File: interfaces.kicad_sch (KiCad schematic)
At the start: 20 parts

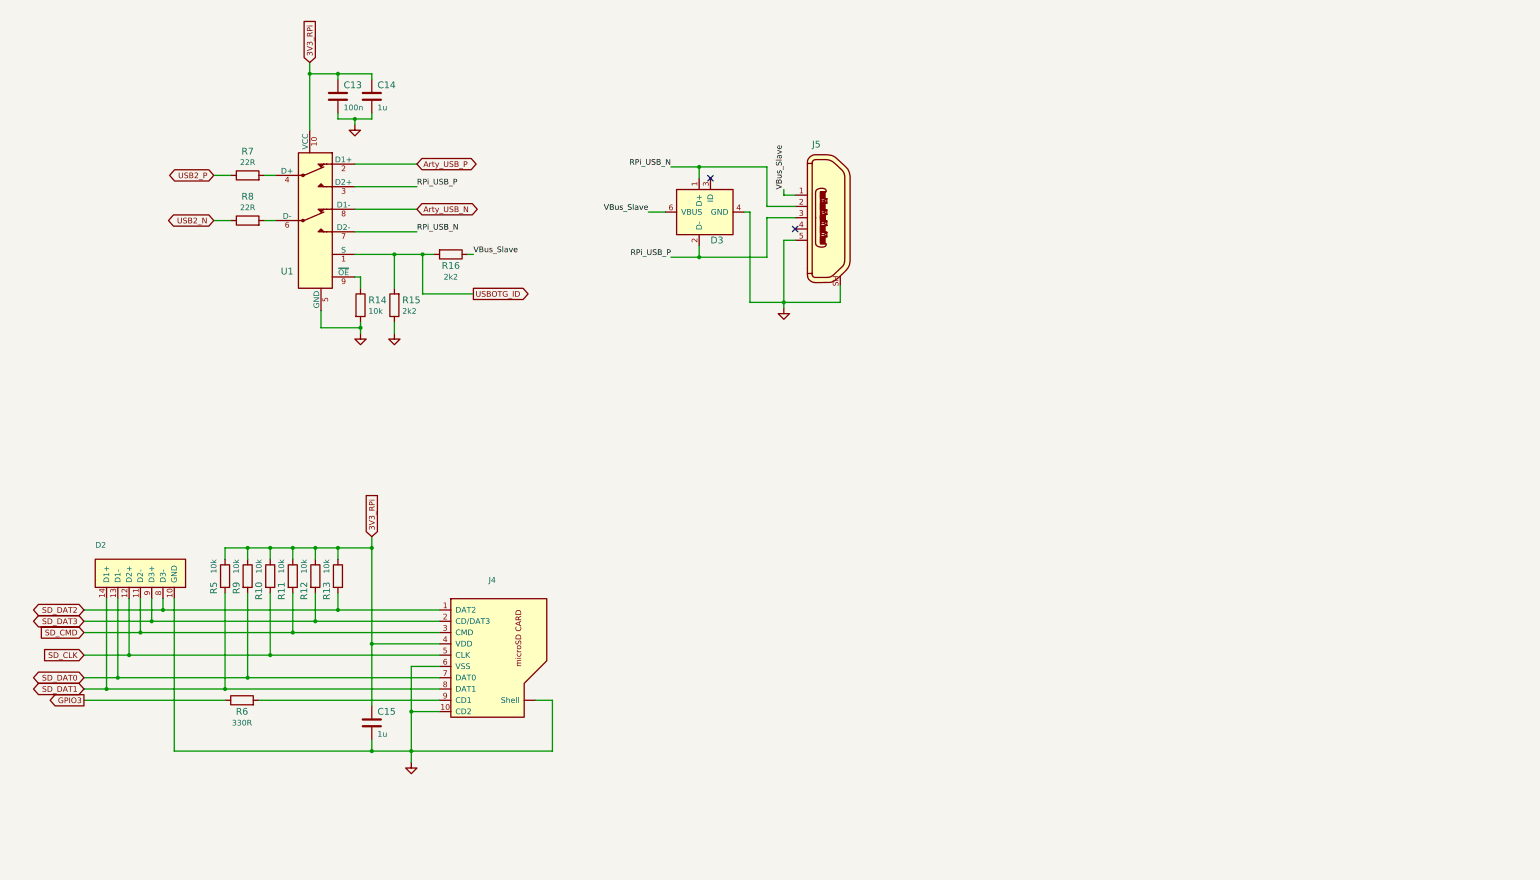
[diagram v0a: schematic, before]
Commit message: Exchanged flyback to CUI DCDC converter on schematics. Added logos.
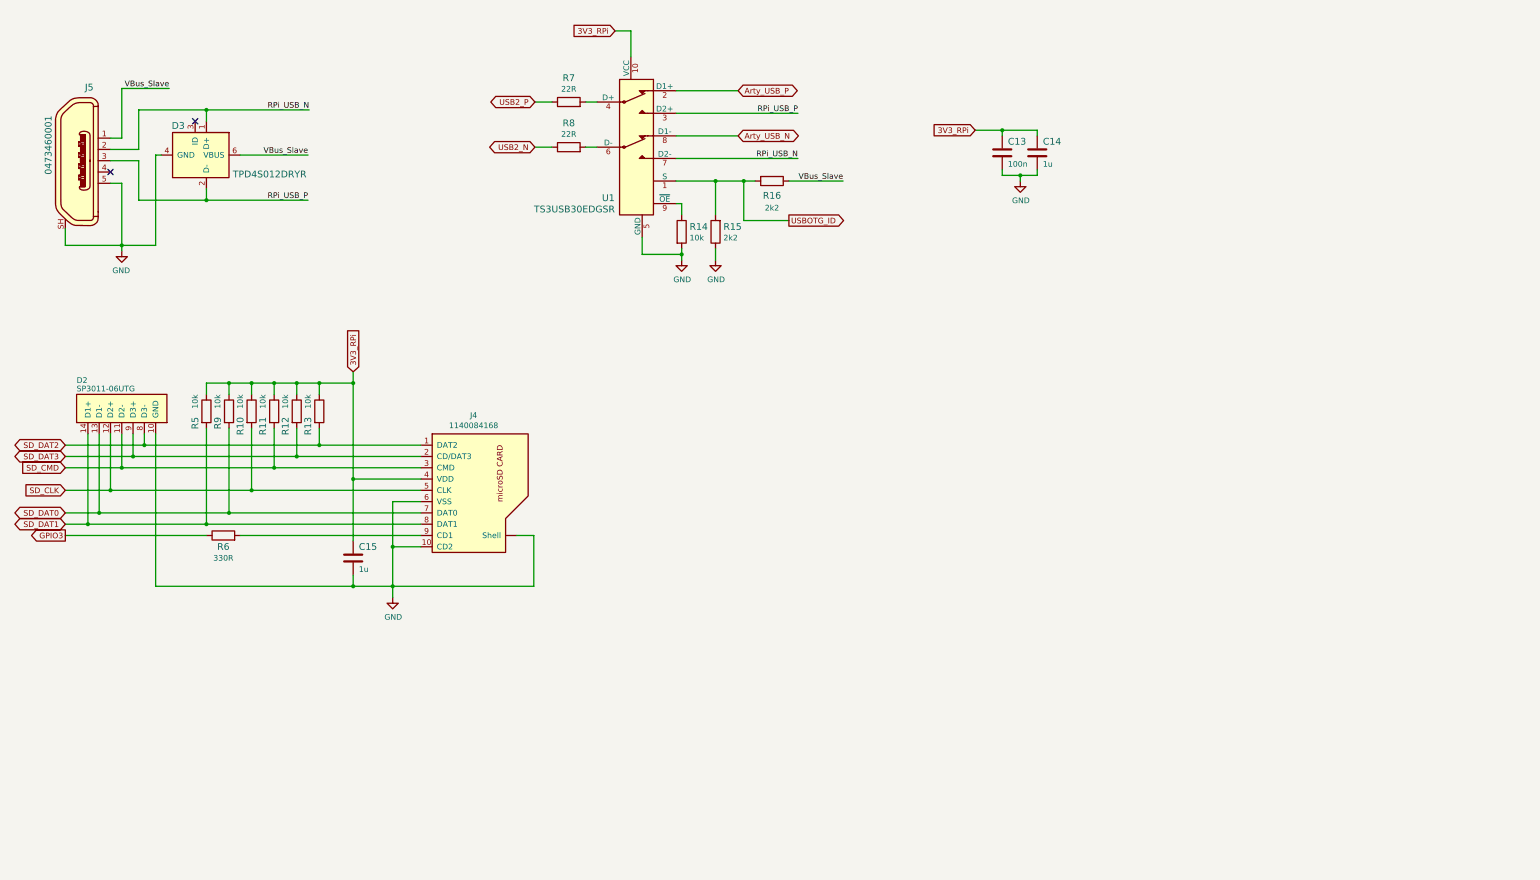
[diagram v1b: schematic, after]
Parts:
- C13: value (none) -> C_100n_0402; footprint scalenode-footprints: -> scalenode-footprints:0402-cap
- C14, C15: value (none) -> C_1u_0402; footprint scalenode-footprints: -> scalenode-footprints:0402-cap
- D2: value (none) -> SP3011-06UTG; footprint scalenode-footprints: -> scalenode-footprints:SON50P350X135X55-14N
- D3: value (none) -> TPD4S012DRYR; footprint scalenode-footprints: -> scalenode-footprints:UFDFN-6_1.45x1mm
- J4: value (none) -> 1140084168; footprint scalenode-footprints: -> scalenode-footprints:MicroSD_1140084168
- J5: value (none) -> 0473460001; footprint scalenode-footprints: -> scalenode-footprints:USB_Micro_B_Female_0473460001
- R10, R11, R12, R13, R14, R5, R9: value (none) -> R_10k_0402; footprint scalenode-footprints: -> scalenode-footprints:0402-res
- R15, R16: value (none) -> R_2k2_0402; footprint scalenode-footprints: -> scalenode-footprints:0402-res
- R6: value (none) -> R_330R_0402; footprint scalenode-footprints: -> scalenode-footprints:0402-res
- R7, R8: value (none) -> R_22R_0402; footprint scalenode-footprints: -> scalenode-footprints:0402-res
- U1: value (none) -> TS3USB30EDGSR; footprint scalenode-footprints: -> scalenode-footprints:MSOP-10_W3mm
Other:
- moved on the sheet: C13, C14, C15, D2, D3, J4, J5, R10, R11, R12, R13, R14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

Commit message: Added text fields with schematic descriptions
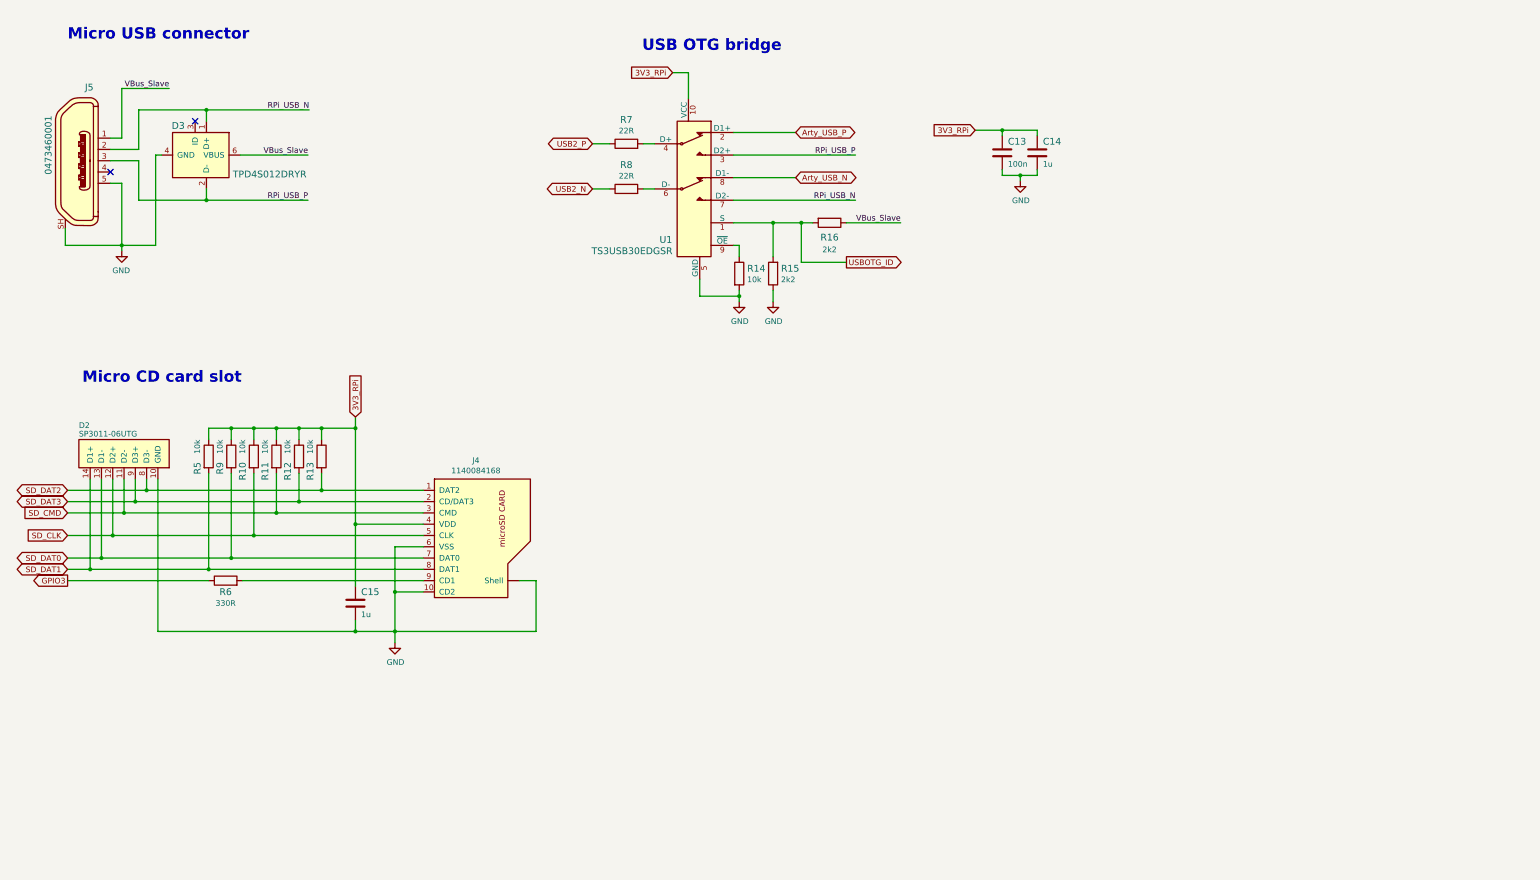
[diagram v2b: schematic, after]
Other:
- note added: "Micro CD card slot"
- note added: "Micro USB connector"
- note added: "USB OTG bridge"
- moved on the sheet: C15, D2, J4, R10, R11, R12, R13, R14, R15, R16, R5, R6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

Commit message: Implemented changes from rev 1.0.4. New components initial placement
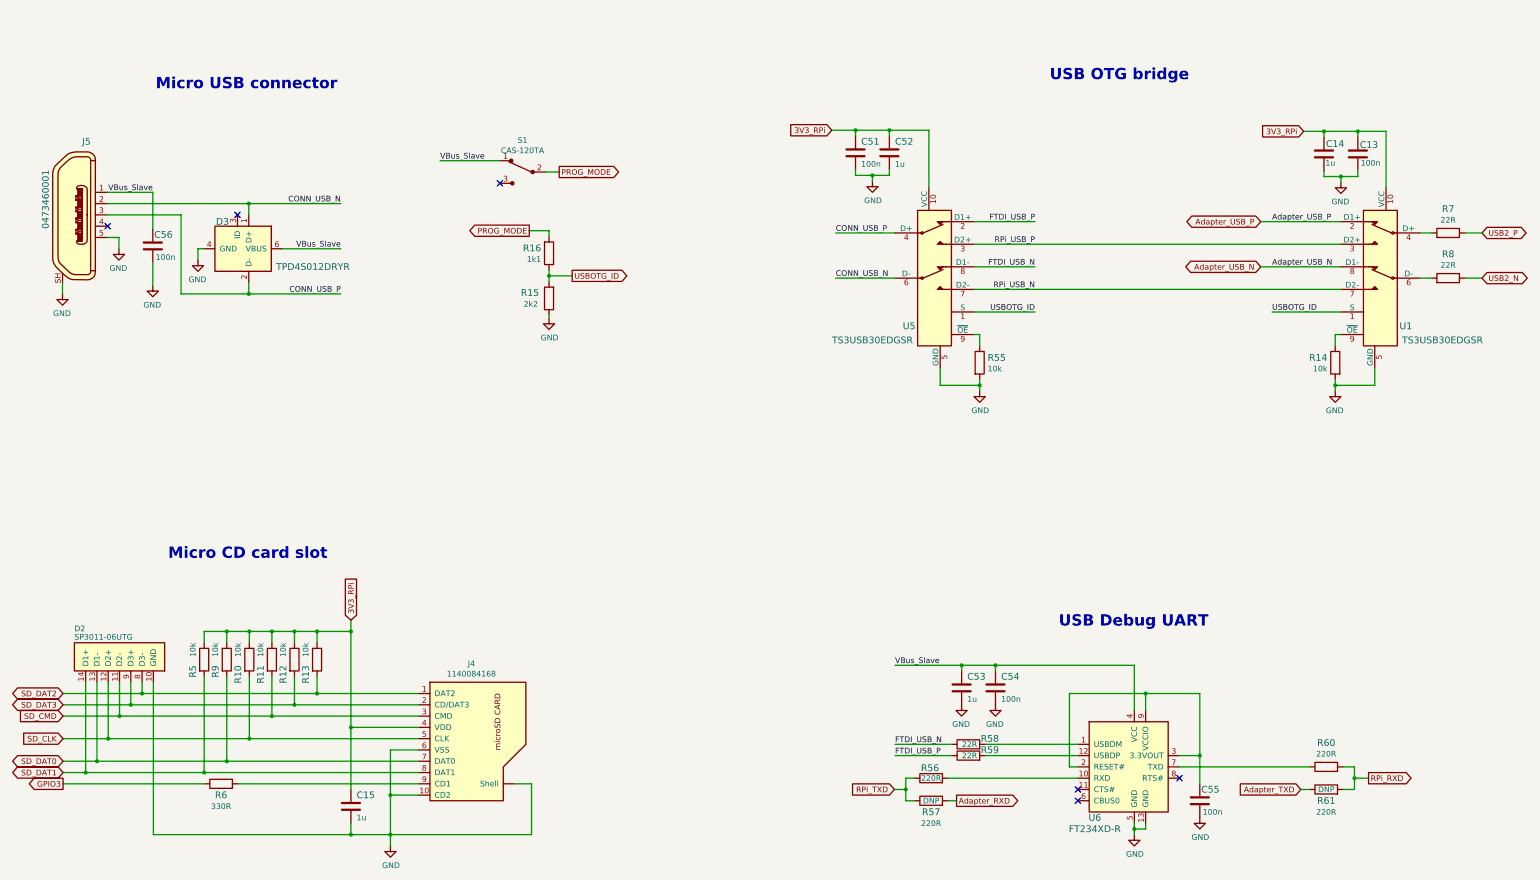
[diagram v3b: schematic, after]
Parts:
- removed R16: R_2k2_0402, scalenode-footprints:0402-res, symbol scalenode:R_2k2_0402
- added C51, C54, C55, C56: C_100n_0402, scalenode-footprints:0402-cap, symbol scalenode:C_100n_0402
- added C52, C53: C_1u_0402, scalenode-footprints:0402-cap, symbol scalenode:C_1u_0402
- added R16: R_1k1_0402, scalenode-footprints:0402-res, symbol scalenode:R_1k1_0402
- added R55: R_10k_0402, scalenode-footprints:0402-res, symbol scalenode:R_10k_0402
- added R56, R57, R60, R61: R_220R_0402, scalenode-footprints:0402-res, symbol scalenode:R_220R_0402
- added R58, R59: R_22R_0402, scalenode-footprints:0402-res, symbol scalenode:R_22R_0402
- added S1: CAS-120TA, scalenode-footprints:Switch_Slide_CAS-120TA, symbol scalenode:CAS-120TA
- added U5: TS3USB30EDGSR, scalenode-footprints:MSOP-10_W3mm, symbol scalenode:TS3USB30EDGSR
- added U6: FT234XD-R, scalenode-footprints:DFN-12-1EP_3x3mm, symbol scalenode:FT234XD-R
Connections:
- net 3V3_RPi: now also C51.1, C52.1, U5.10 (VCC)
- net GND: now also C51.2, C52.2, C53.2, C54.2, C55.2, C56.2, R55.2, U5.5 (GND), U6.13 (GND), U6.5 (GND)
- net RPi_USB_N: now also U5.7 (D2-); no longer D3.1 (D+), J5.2
- net RPi_USB_P: now also U5.3 (D2+); no longer D3.2 (D-), J5.3
- net USBOTG_ID: now also R16.1, U5.1 (S)
- net VBus_Slave: now also C53.1, C54.1, C56.1, S1.1, U6.4 (VCC)
- net Arty_USB_N renamed Adapter_USB_N
- net Arty_USB_P renamed Adapter_USB_P
- new net: R55.1, U5.9 (~{OE})
- new net: R58.2, U6.1 (USBDM)
- new net: R56.2, U6.10 (RXD)
- new net: R59.2, U6.12 (USBDP)
- new net: C55.1, U6.2 (RESET#), U6.3 (3.3VOUT), U6.9 (VCCIO)
- new net: R60.1, U6.7 (TXD)
- new net Adapter_RXD: R57.2
- new net Adapter_TXD: R61.1
- new net CONN_USB_N: D3.1 (D+), J5.2, U5.6 (D-)
- new net CONN_USB_P: D3.2 (D-), J5.3, U5.4 (D+)
- new net FTDI_USB_N: R58.1, U5.8 (D1-)
- new net FTDI_USB_P: R59.1, U5.2 (D1+)
- new net PROG_MODE: R16.2, S1.2
- new net RPi_RXD: R60.2, R61.2
- new net RPi_TXD: R56.1, R57.1
- no-connect marks 2 -> 6
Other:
- note added: "USB Debug UART"
- moved on the sheet: C13, C14, C15, D2, D3, J4, J5, R10, R11, R12, R13, R14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

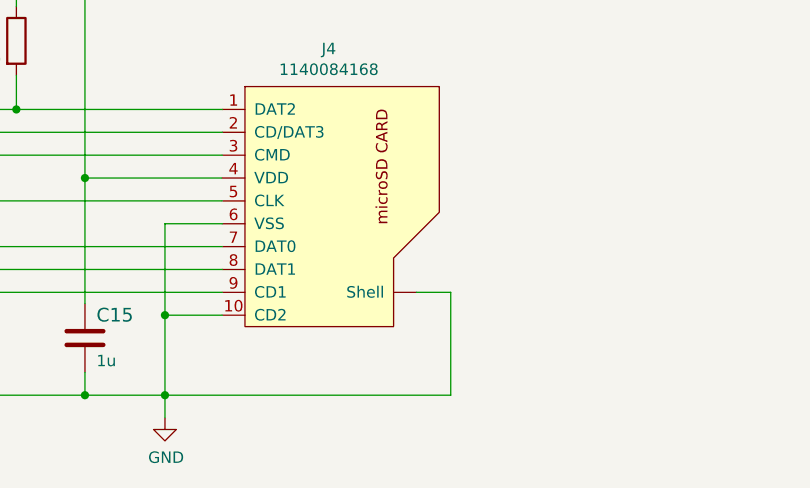
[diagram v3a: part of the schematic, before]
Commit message: Optimized routes. Added missing 3D models
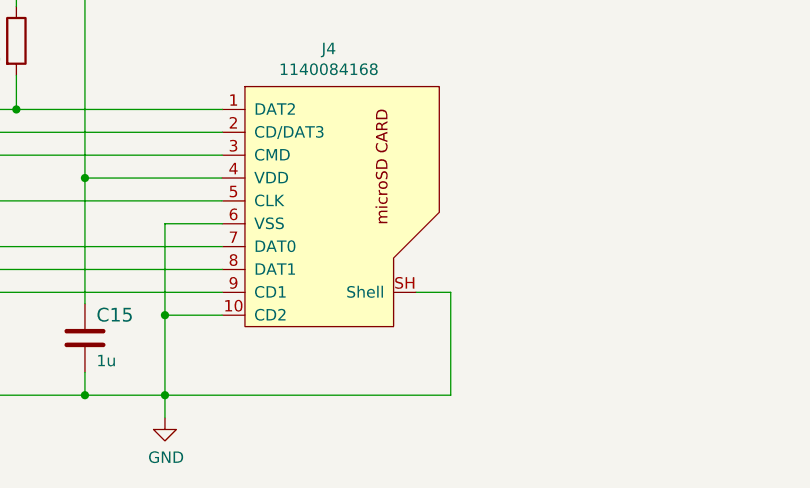
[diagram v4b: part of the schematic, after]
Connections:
- net GND: now also J4.SH (Shell); no longer J4.~ (Shell)
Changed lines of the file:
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@@
     (pin "8")
     (pin "9")
-    (pin "~")
+    (pin "SH")
   )
   (symbol (lib_id "scalenode:GND") (at 111.506 208.026 0) (unit 1)

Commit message: Rename project files
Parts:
- C13, C51, C54, C55, C56: footprint scalenode-footprints:0402-cap -> scalenode-cm4-baseboard-footprints:0402-cap; symbol scalenode:C_100n_0402 -> scalenode-cm4-baseboard:C_100n_0402
- C14, C15, C52, C53: footprint scalenode-footprints:0402-cap -> scalenode-cm4-baseboard-footprints:0402-cap; symbol scalenode:C_1u_0402 -> scalenode-cm4-baseboard:C_1u_0402
- D2: footprint scalenode-footprints:SON50P350X135X55-14N -> scalenode-cm4-baseboard-footprints:SON50P350X135X55-14N; symbol scalenode:SP3011-06UTG -> scalenode-cm4-baseboard:SP3011-06UTG
- D3: footprint scalenode-footprints:UFDFN-6_1.45x1mm -> scalenode-cm4-baseboard-footprints:UFDFN-6_1.45x1mm; symbol scalenode:TPD4S012DRYR -> scalenode-cm4-baseboard:TPD4S012DRYR
- J4: footprint scalenode-footprints:MicroSD_1140084168 -> scalenode-cm4-baseboard-footprints:MicroSD_1140084168; symbol scalenode:1140084168 -> scalenode-cm4-baseboard:1140084168
- J5: footprint scalenode-footprints:USB_Micro_B_Female_0473460001 -> scalenode-cm4-baseboard-footprints:USB_Micro_B_Female_0473460001; symbol scalenode:0473460001 -> scalenode-cm4-baseboard:0473460001
- R10, R11, R12, R13, R14, R5, R55, R9: footprint scalenode-footprints:0402-res -> scalenode-cm4-baseboard-footprints:0402-res; symbol scalenode:R_10k_0402 -> scalenode-cm4-baseboard:R_10k_0402
- R15: footprint scalenode-footprints:0402-res -> scalenode-cm4-baseboard-footprints:0402-res; symbol scalenode:R_2k2_0402 -> scalenode-cm4-baseboard:R_2k2_0402
- R16: footprint scalenode-footprints:0402-res -> scalenode-cm4-baseboard-footprints:0402-res; symbol scalenode:R_1k1_0402 -> scalenode-cm4-baseboard:R_1k1_0402
- R56, R57, R60, R61: footprint scalenode-footprints:0402-res -> scalenode-cm4-baseboard-footprints:0402-res; symbol scalenode:R_220R_0402 -> scalenode-cm4-baseboard:R_220R_0402
- R58, R59, R7, R8: footprint scalenode-footprints:0402-res -> scalenode-cm4-baseboard-footprints:0402-res; symbol scalenode:R_22R_0402 -> scalenode-cm4-baseboard:R_22R_0402
- R6: footprint scalenode-footprints:0402-res -> scalenode-cm4-baseboard-footprints:0402-res; symbol scalenode:R_330R_0402 -> scalenode-cm4-baseboard:R_330R_0402
- S1: footprint scalenode-footprints:Switch_Slide_CAS-120TA -> scalenode-cm4-baseboard-footprints:Switch_Slide_CAS-120TA; symbol scalenode:CAS-120TA -> scalenode-cm4-baseboard:CAS-120TA
- U1, U5: footprint scalenode-footprints:MSOP-10_W3mm -> scalenode-cm4-baseboard-footprints:MSOP-10_W3mm; symbol scalenode:TS3USB30EDGSR -> scalenode-cm4-baseboard:TS3USB30EDGSR
- U6: footprint scalenode-footprints:DFN-12-1EP_3x3mm -> scalenode-cm4-baseboard-footprints:DFN-12-1EP_3x3mm; symbol scalenode:FT234XD-R -> scalenode-cm4-baseboard:FT234XD-R
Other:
- title: Scalenode -> Scalenode CM4 Baseboard
